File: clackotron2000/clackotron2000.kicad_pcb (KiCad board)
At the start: 2 copper layers, 73.5 x 65 mm, 59 parts, among them J3 Conn_ESP_Prog, J4 Power, J5 Output, J6 Conn_01x04, Q1 BSN20, Q2 BSN20, Q3 BSN20, Q4 BSN20, SW1 SW_Push_DPDT, SW2 SW_Push, SW3 SW_Push, U1 ESP32-WROOM-32, U2 SP3485EN, U3 R-78B5.0-1.0, U4 PCF85263ATT, U5 AMS1117-3.3, Y1 Crystal

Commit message: chore: rebase changes from internal repository
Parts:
- added REF**: MountingHole_3.2mm_M3, MountingHole:MountingHole_3.2mm_M3, F.Cu at (127.0, 90.0)
- added REF**: MountingHole_3.2mm_M3, MountingHole:MountingHole_3.2mm_M3, F.Cu at (166.0, 128.5)
- added REF**: MountingHole_3.2mm_M3, MountingHole:MountingHole_3.2mm_M3, F.Cu at (175.0, 85.0)
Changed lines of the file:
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@@
     )
   )
+  (footprint "MountingHole:MountingHole_3.2mm_M3" (layer "F.Cu")
+    (at 127 90)
+    (descr "Mounting Hole 3.2mm, no annular, M3")
+    (tags "mounting hole 3.2mm no annular m3")
+    (attr exclude_from_pos_files exclude_from_bom)
+    (fp_text reference "REF**" (at 0 -4.2) (layer "F.SilkS") hide
+        (effects (font (size 1 1) (thickness 0.15)))
+    )
+    (fp_text value "MountingHole_3.2mm_M3" (at 0 4.2) (layer "F.Fab")
+        (effects (font (size 1 1) (thickness 0.15)))
+    )
+    (fp_text user "${REFERENCE}" (at 0 0) (layer "F.Fab")
+        (effects (font (size 1 1) (thickness 0.15)))
+    )
+    (fp_circle (center 0 0) (end 3.2 0)
+      (stroke (width 0.15) (type solid)) (fill none) (layer "Cmts.User"))
+    (fp_circle (center 0 0) (end 3.45 0)
+      (stroke (width 0.05) (type solid)) (fill none) (layer "F.CrtYd"))
+    (pad "" np_thru_hole circle (at 0 0) (size 3.2 3.2) (drill 3.2) (layers "*.Cu" "*.Mask"))
+  )
   (footprint "Connector_PinHeader_2.54mm:PinHeader_2x03_P2.54mm_Vertical" (layer "F.Cu")
     (at 116.078 74.549)
@@
     )
   )
+  (footprint "MountingHole:MountingHole_3.2mm_M3" (layer "F.Cu")
+    (at 166 128.5)
+    (descr "Mounting Hole 3.2mm, no annular, M3")
+    (tags "mounting hole 3.2mm no annular m3")
+    (attr exclude_from_pos_files exclude_from_bom)
+    (fp_text reference "REF**" (at 0 -4.2) (layer "F.SilkS") hide
+        (effects (font (size 1 1) (thickness 0.15)))
+    )
+    (fp_text value "MountingHole_3.2mm_M3" (at 0 4.2) (layer "F.Fab")
+        (effects (font (size 1 1) (thickness 0.15)))
+    )
+    (fp_text user "${REFERENCE}" (at 0 0) (layer "F.Fab")
+        (effects (font (size 1 1) (thickness 0.15)))
+    )
+    (fp_circle (center 0 0) (end 3.2 0)
+      (stroke (width 0.15) (type solid)) (fill none) (layer "Cmts.User"))
+    (fp_circle (center 0 0) (end 3.45 0)
+      (stroke (width 0.05) (type solid)) (fill none) (layer "F.CrtYd"))
+    (pad "" np_thru_hole circle (at 0 0) (size 3.2 3.2) (drill 3.2) (layers "*.Cu" "*.Mask"))
+  )
   (footprint "Resistor_SMD:R_0805_2012Metric" (layer "F.Cu")
     (at 167.955 84.3765 180)
@@
     )
   )
+  (footprint "MountingHole:MountingHole_3.2mm_M3" (layer "F.Cu")
+    (at 175 85)
+    (descr "Mounting Hole 3.2mm, no annular, M3")
+    (tags "mounting hole 3.2mm no annular m3")
+    (attr exclude_from_pos_files exclude_from_bom)
+    (fp_text reference "REF**" (at 0 -4.2) (layer "F.SilkS") hide
+        (effects (font (size 1 1) (thickness 0.15)))
+    )
+    (fp_text value "MountingHole_3.2mm_M3" (at 0 4.2) (layer "F.Fab")
+        (effects (font (size 1 1) (thickness 0.15)))
+    )
+    (fp_text user "${REFERENCE}" (at 0 0) (layer "F.Fab")
+        (effects (font (size 1 1) (thickness 0.15)))
+    )
+    (fp_circle (center 0 0) (end 3.2 0)
+      (stroke (width 0.15) (type solid)) (fill none) (layer "Cmts.User"))
+    (fp_circle (center 0 0) (end 3.45 0)
+      (stroke (width 0.05) (type solid)) (fill none) (layer "F.CrtYd"))
+    (pad "" np_thru_hole circle (at 0 0) (size 3.2 3.2) (drill 3.2) (layers "*.Cu" "*.Mask"))
+  )
   (footprint "Capacitor_SMD:C_0805_2012Metric" (layer "F.Cu")

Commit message: hardware redesign for v3.0 done
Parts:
- removed C16: 47uF/35V, JLCPCB:CAP-SMD_BD6.3-L6.6-W6.6-LS7.2-FD
- removed J4: Power, TerminalBlock_4Ucon:TerminalBlock_4Ucon_1x02_P3.50mm_Horizontal
- removed J5: Output, TerminalBlock_4Ucon:TerminalBlock_4Ucon_1x04_P3.50mm_Horizontal
- removed J6: Conn_01x04, JLCPCB:CONN-SMD_SM04B-SURS-TF-LF-SN
- removed the REF** at (127.0, 90.0)
- removed the REF** at (166.0, 128.5)
- removed the REF** at (175.0, 85.0)
- removed SW3: SW_Push, JLCPCB:SW-SMD_4P-L6.0-W6.0-P4.50-LS10.0-BL
- added D7: 1N4007, Diode_SMD:D_SMA, F.Cu at (126.2, 86.6)
- added J1: Conn_ESP_Prog, Connector_PinHeader_2.54mm:PinHeader_2x03_P2.54mm_Vertical, F.Cu at (128.9, 71.0)
- added J2: Power, TerminalBlock_4Ucon:TerminalBlock_4Ucon_1x02_P3.50mm_Horizontal, F.Cu at (114.9, 96.3)
- added REF**: MountingHole_3.2mm_M3, MountingHole:MountingHole_3.2mm_M3, F.Cu at (119.6, 72.0)
- added REF**: MountingHole_3.2mm_M3, MountingHole:MountingHole_3.2mm_M3, F.Cu at (179.6, 72.0)
- added REF**: MountingHole_3.2mm_M3, MountingHole:MountingHole_3.2mm_M3, F.Cu at (126.6, 127.0)
- added REF**: MountingHole_3.2mm_M3, MountingHole:MountingHole_3.2mm_M3, F.Cu at (159.6, 127.0)
- added USBC1: USB3.1C16PFSMT, clackotron_fp:USB-C-SMD_TYPE-C-USB-17, F.Cu at (115.2, 81.1)
- C11: value 1uF -> 22uF; footprint Capacitor_SMD:C_0805_2012Metric -> Capacitor_SMD:C_1206_3216Metric
- C12: value 22uF -> 100nF; footprint Capacitor_SMD:C_1206_3216Metric -> Capacitor_SMD:C_0805_2012Metric
- C2, C5, C9: value 100nF -> 1uF
- C4, C7: value 1uF -> 100nF
- C8: value 100nF -> 47uF/35V; footprint Capacitor_SMD:C_0805_2012Metric -> JLCPCB:CAP-SMD_BD6.3-L6.6-W6.6-LS7.2-FD
- D2: value 1N4007 -> LESD5D5.0CT1G; footprint Diode_SMD:D_SMA -> clackotron_fp:SOD-523_L1.2-W0.8-LS1.6-BI
- D3, D5: value LED -> LESD5D5.0CT1G; footprint LED_SMD:LED_0805_2012Metric -> clackotron_fp:SOD-523_L1.2-W0.8-LS1.6-BI
- D4: value LED -> 1N4007; footprint LED_SMD:LED_0805_2012Metric -> Diode_SMD:D_SMA
- D6: value WS2812B -> LED; footprint LED_SMD:LED_WS2812B_PLCC4_5.0x5.0mm_P3.2mm -> LED_SMD:LED_0805_2012Metric
- J3: value Conn_ESP_Prog -> Output; footprint Connector_PinHeader_2.54mm:PinHeader_2x03_P2.54mm_Vertical -> TerminalBlock_4Ucon:TerminalBlock_4Ucon_1x04_P3.50mm_Horizontal
- R10: value 2k2 -> 10k
- R12, R13, R14: value 10k -> 2k2
- R17: value 220R -> 10k; footprint Resistor_SMD:R_1206_3216Metric -> Resistor_SMD:R_0805_2012Metric
- R5, R6: value 1k1 -> 5.1k
- R7: value 1k1 -> 10k
- R8: value 2k2 -> 220R; footprint Resistor_SMD:R_0805_2012Metric -> Resistor_SMD:R_1206_3216Metric
- R9: value 2k2 -> 1k1
- SW1: value SW_Push_DPDT -> K2-1102SP-C4SC-04; footprint clackotron_fp:SW_Push_DPDT -> clackotron_fp:KEY-SMD_4P-L6.0-W6.0-P4.50-LS9.5-BL
- SW2: value SW_Push -> K2-1102SP-C4SC-04; footprint JLCPCB:SW-SMD_4P-L6.0-W6.0-P4.50-LS10.0-BL -> clackotron_fp:KEY-SMD_4P-L6.0-W6.0-P4.50-LS9.5-BL
- U1: value ESP32-WROOM-32 -> PCF85263ATT; footprint RF_Module:ESP32-WROOM-32 -> Package_SO:TSSOP-8_3x3mm_P0.65mm
- U2: value SP3485EN -> ESP32-S3-WROOM-1(N8R2); footprint Package_SO:SOIC-8_3.9x4.9mm_P1.27mm -> clackotron_fp:WIRELM-SMD_ESP32-S3-WROOM-1
- U3: value R-78B5.0-1.0 -> SP3485EN; footprint Converter_DCDC:Converter_DCDC_RECOM_R-78E-0.5_THT -> Package_SO:SOIC-8_3.9x4.9mm_P1.27mm
- U4: value PCF85263ATT -> R-78B5.0-1.0; footprint Package_SO:TSSOP-8_3x3mm_P0.65mm -> Converter_DCDC:Converter_DCDC_RECOM_R-78E-0.5_THT
- moved U4 67.1 mm to (116.0, 111.5), turned to 0 degrees
- moved D6 55.9 mm to (123.9, 83.7), turned to 0 degrees
- moved C9 49.8 mm to (115.1, 101.0)
- moved D3 49.6 mm to (120.4, 81.9), turned to 90 degrees
- moved C4 47.1 mm to (176.6, 86.9), turned to 180 degrees
- moved R2 46.3 mm to (145.8, 80.5), turned to 0 degrees
- moved R5 45.8 mm to (120.2, 85.2), turned to 90 degrees
- moved J3 43.7 mm to (116.4, 118.2), turned to -90 degrees
- moved C5 42.8 mm to (143.0, 75.2), turned to -90 degrees
- moved C7 42.7 mm to (143.5, 119.7), turned to 0 degrees
- moved R1 42.6 mm to (175.0, 93.2), turned to 180 degrees
- moved C2 42.3 mm to (176.6, 84.7), turned to 180 degrees
- moved R9 41.6 mm to (127.4, 83.7)
- moved D5 38.2 mm to (116.1, 87.3)
- moved R10 36.3 mm to (150.8, 118.1)
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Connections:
- C1 pad 1: +5V -> +3V3
- C11 pad 1: +VDC -> +5V
- C2 pad 1: EN -> +3V3
- C3 pad 1: +3V3 -> EN
- C5 pad 1: Net-(BT1-+) -> +3V3
- C6 pad 1: +3V3 -> Net-(BT1-+)
- C7 pad 1: +3V3 -> +5V
- C8 pad 1: +5V -> +VDC
- C9 pad 1: +5V -> +VDC
- D1 pad 2: Net-(D1-DOUT) -> unconnected-(D1-DOUT-Pad2)
- D2 pad 1: Net-(D2-K) -> GND
- D2 pad 2: Net-(D2-A) -> D-
- D3 pad 2: Net-(D3-A) -> D+
- D4 pad 1: GND -> +VDC
- D5 pad 2: Net-(D5-A) -> VBUS
- D6 pad 1: +5V -> GND
- D6 pad 2: unconnected-(D6-DOUT-Pad2) -> Net-(D6-A)
- J3 pad 1: TXD0 -> RS485_A
- J3 pad 2: +3V3 -> RS485_B
- J3 pad 3: IO0 -> GND
- J3 pad 4: RXD0 -> +VDC
- R1 pad 1: +3V3 -> Net-(U1-OSCI)
- R1 pad 2: Button2 -> Net-(R1-Pad2)
- R10 pad 2: DataTX -> Button2
- R11 pad 2: LED_Data -> DataRX
- R12 pad 1: +5V -> +3V3
- R12 pad 2: DataRX_5V -> DataEN
- R13 pad 1: +5V -> +3V3
- R13 pad 2: DataEN_5V -> DataTX
- R14 pad 1: +5V -> +3V3
- R14 pad 2: DataTX_5V -> LED_Data
- R15 pad 2: LED_Data_5V -> DataRX_5V
- R16 pad 1: +3V3 -> +5V
- R16 pad 2: EN -> DataEN_5V
- R17 pad 1: RS485_A -> +5V
- R17 pad 2: RS485_B -> DataTX_5V
- R18 pad 1: Net-(U4-OSCI) -> +5V
- R18 pad 2: Net-(R18-Pad2) -> LED_Data_5V
- R2 pad 2: Button1 -> EN
- R3 pad 2: SCK -> SCL
- R5 pad 1: LED2 -> GND
- R5 pad 2: Net-(D3-A) -> Net-(USBC1-CC2)
- R6 pad 1: +5V -> Net-(USBC1-CC1)
- R6 pad 2: Net-(D4-A) -> GND
- R7 pad 1: LED1 -> +3V3
- R7 pad 2: Net-(D5-A) -> Button1
- R8 pad 1: +3V3 -> RS485_A
- R8 pad 2: DataRX -> RS485_B
- R9 pad 1: +3V3 -> +5V
- R9 pad 2: DataEN -> Net-(D6-A)
- SW1 pad 1: unconnected-(SW1-A-Pad1) -> Button1
- SW1 pad 2: Net-(D2-K) -> Button1
- SW1 pad 3: +VDC -> GND
- SW1 pad 4: unconnected-(SW1-A-Pad4) -> GND
- SW2 pad 1: Button1 -> Button2
- SW2 pad 2: Button1 -> Button2
- U1 pad 1: GND -> Net-(U1-OSCI)
- U1 pad 2: +3V3 -> Net-(U1-OSCO)
- U1 pad 3: EN -> Net-(BT1-+)
- U1 pad 4: unconnected-(U1-SENSOR_VP-Pad4) -> GND
- U1 pad 5: unconnected-(U1-SENSOR_VN-Pad5) -> SDA
- U1 pad 6: unconnected-(U1-IO34-Pad6) -> SCL
- U1 pad 8: unconnected-(U1-IO32-Pad8) -> +3V3
- U2 pad 1: DataRX_5V -> GND
- U2 pad 2: DataEN_5V -> +3V3
- U2 pad 3: DataEN_5V -> EN
- U2 pad 4: DataTX_5V -> unconnected-(U2-IO4-Pad4)
- U2 pad 5: GND -> unconnected-(U2-IO5-Pad5)
- U2 pad 6: RS485_A -> unconnected-(U2-IO6-Pad6)
- U2 pad 7: RS485_B -> unconnected-(U2-IO7-Pad7)
- U2 pad 8: +5V -> LED_Data
- U3 pad 1: +VDC -> DataRX_5V
- U3 pad 2: GND -> DataEN_5V
- U3 pad 3: +5V -> DataEN_5V
- U4 pad 1: Net-(U4-OSCI) -> +VDC
- U4 pad 2: Net-(U4-OSCO) -> GND
- U4 pad 3: Net-(BT1-+) -> +5V
- Y1 pad 1: Net-(R18-Pad2) -> Net-(R1-Pad2)
- Y1 pad 2: Net-(U4-OSCO) -> Net-(U1-OSCO)
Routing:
- net Button1: track 59.1 -> 140.3 mm, vias 2 -> 1
- net IO0: track 56.7 -> 0.00 mm, vias 1 -> 0
- net LED2: track 47.1 -> 0.00 mm, vias 2 -> 0
- net D-: track 0.00 -> 42.5 mm, vias 0 -> 2
- net D+: track 0.00 -> 41.9 mm, vias 0 -> 2
- net SCK: track 40.9 -> 0.00 mm
- net Net-(D1-DOUT): track 40.0 -> 0.00 mm, vias 2 -> 0
- net LED1: track 37.9 -> 0.00 mm, vias 2 -> 0
- net VBUS: track 0.00 -> 24.0 mm
- net +3V3: track 195.0 -> 216.6 mm, vias 4 -> 10
- net SCL: track 0.00 -> 20.6 mm, vias 0 -> 2
- net Button2: track 68.3 -> 49.2 mm, vias 2 -> 0
- net LED_Data_5V: track 61.5 -> 43.2 mm, vias 4 -> 0
- net Net-(D2-K): track 18.2 -> 0.00 mm
- net SDA: track 37.5 -> 19.6 mm
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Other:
- board text added: "${url}"
- board text added: "MODE"
- board text added: "RESET"

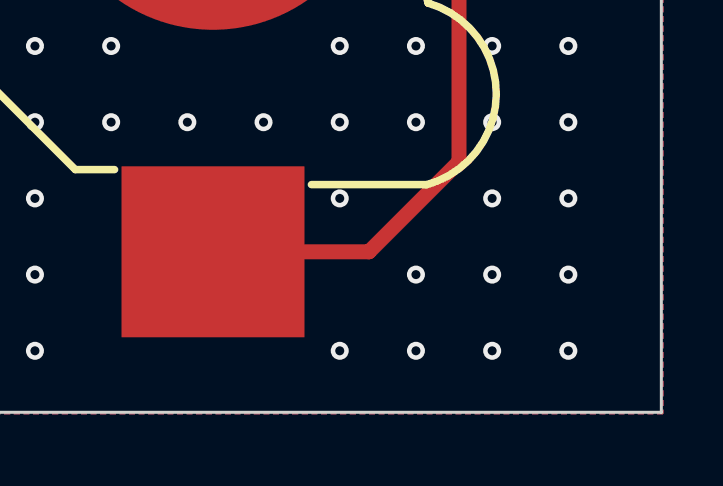
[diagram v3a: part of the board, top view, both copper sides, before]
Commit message: add oshw logo and fix some pcb part configs
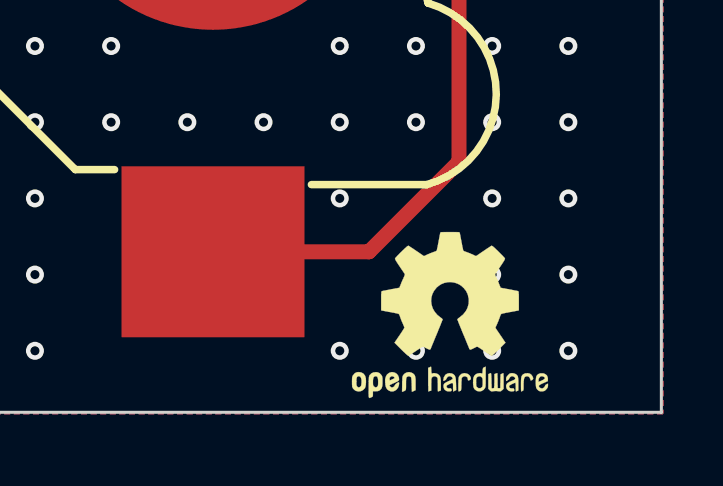
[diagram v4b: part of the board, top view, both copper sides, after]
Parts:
- added REF**: OSHW-Logo2_7.3x6mm_SilkScreen, Symbol:OSHW-Logo2_7.3x6mm_SilkScreen, F.Cu at (176.9, 129.6)

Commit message: changed all parts. set to version 3.1
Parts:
- U1: value PCF85263ATT -> PCF85263ATL; footprint Package_SO:TSSOP-8_3x3mm_P0.65mm -> Package_DFN_QFN:DFN-10-1EP_2.6x2.6mm_P0.5mm_EP1.3x2.2mm
- moved U1 0.92 mm to (179.2, 90.4)
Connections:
- U1 pad 4: GND -> unconnected-(U1-TS_(CLK/INTB)-Pad4)
- U1 pad 5: SDA -> GND
- U1 pad 6: SCL -> SDA
- U1 pad 7: unconnected-(U1-~{INTA}-Pad7) -> SCL
- U1 pad 8: +3V3 -> unconnected-(U1-CLK-Pad8)
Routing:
- net GND: track 65.7 -> 74.1 mm
- net Net-(BT1-+): track 49.7 -> 51.5 mm
- net Net-(U1-OSCO): track 3.03 -> 4.83 mm
- net Net-(U1-OSCI): track 1.97 -> 3.37 mm
